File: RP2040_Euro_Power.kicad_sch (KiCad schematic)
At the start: 150 parts, among them J1 Conn_01x40, J2 Conn_01x40, J3 Power, J4 USB C/USB 2.0, J5 Conn_01x03_Pin, SW1 SW_BOOT, SW2 SW_RESET, U1 78L05_SOT89, U2 W25Q128JVS, U3 TL431D, U4 AMS1117-3.3, U5 RP2040, U6 MCP6002, Y1 Crystal_12MHz_4Pin

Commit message: half of the parts placed on board
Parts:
- removed JP127, JP128, JP129, JP130: ~, Jumper:SolderJumper-2_P1.3mm_Bridged_RoundedPad1.0x1.5mm, symbol Jumper:SolderJumper_2_Bridged
- removed U6: MCP6002, Package_SO:SOIC-8_3.9x4.9mm_P1.27mm, symbol winterbloom:MCP6002
- added C25: 100n, winterbloom:C_0603_HandSolder, symbol DecapodDevices:C_Small
- added D11, D13: D_Schottky, winterbloom:D_SMA, symbol Diode:1N5819
- added JP127, JP128, JP129, JP130: SolderJumper_2_Open, Jumper:SolderJumper-2_P1.3mm_Open_RoundedPad1.0x1.5mm, symbol Jumper:SolderJumper_2_Open
- added U7: TL072, Package_SO:SOIC-8_3.9x4.9mm_P1.27mm, symbol Amplifier_Operational:TL072
- R8: value 33k -> 47k
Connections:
- net GND_PLANE is gone; now on net GND: JP133.2 (B), JP134.2 (B), JP173.1 (A), JP174.1 (A)
- net RUN is gone; now on net D29: R6.1, SW2.1 (A), U5.26 (RUN)
- net SWCLK is gone; now on net D27: J5.1 (Pin_1), U5.24 (SWCLK)
- net SWD is gone; now on net D28: J5.3 (Pin_3), U5.25 (SWD)
- net +12V: now also C19.1, D2.2 (A), D11.1 (K), U7.8 (V+); no longer R16.1
- net +3.3V: now also D10.2 (A); no longer R20.1
- net +5V: now also D8.2 (A); no longer C19.1, R18.1
- net -12V: now also D7.1 (K), C25.1, D13.2 (A), U7.4 (V-); no longer R17.1
- net D27: now also JP127.1 (A)
- net D28: now also JP128.1 (A)
- net D29: now also JP129.1 (A)
- net GND: now also R16.2, R17.2, R18.2, R19.2, R20.2, C25.2, U7.5 (+); no longer D10.1 (K), D2.1 (K), D7.2 (A), D8.1 (K), D9.1 (K)
- net VBUS: now also D9.2 (A); no longer R19.1
- net at J1.27 (Pin_27): now also JP127.2 (B)
- net at R9.2, U3.1 (K), U3.8 (REF): now also U7.3 (+)
- net at C22.1, R7.1, R8.2: now also U7.2 (-)
- net BOOT: now reaches R2.1, R3.2, R5.1, SW1.1 (A)
- net BOOT: now also JP130.1 (A)
- net at J1.28 (Pin_28): now also JP128.2 (B)
- net at J1.29 (Pin_29): now also JP129.2 (B)
- net at J1.30 (Pin_30): now also JP130.2 (B)
- net at D3.2 (A), FB1.1: now also D13.1 (K)
- net at D4.1 (K), FB2.1: now also D11.2 (A)
- net 3.3VREF renamed 3VREF
- net 3VREF: now also U7.1
- new net: D9.1 (K), R19.1
- new net: D7.2 (A), R17.1
- new net: D2.1 (K), R16.1
- new net: D10.1 (K), R20.1
- new net: D8.1 (K), R18.1
- new net: U7.6 (-), U7.7
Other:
- note added: "Find a use for the extra op amp? Prototyping area if extra space? Add Default/RGB LEDs? Add any niceties for this situation?"
- note added: "No Obvious Problems"
- note removed: "Add Power LEDs Find a use for the extra op amp? Prototyping area if extra space? Figure out SWD/debug stuff"
- note removed: "How should I power 3.3vref buffer? If I use 3.3vreg, I have no headroom for stability If I use 5v, I have to have USB Connected? If I use 12v, op amp will blow up."
- moved on the sheet: C19, C20, C21, C23, C24, C5, C6, C7, C8, D10, D2, D3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

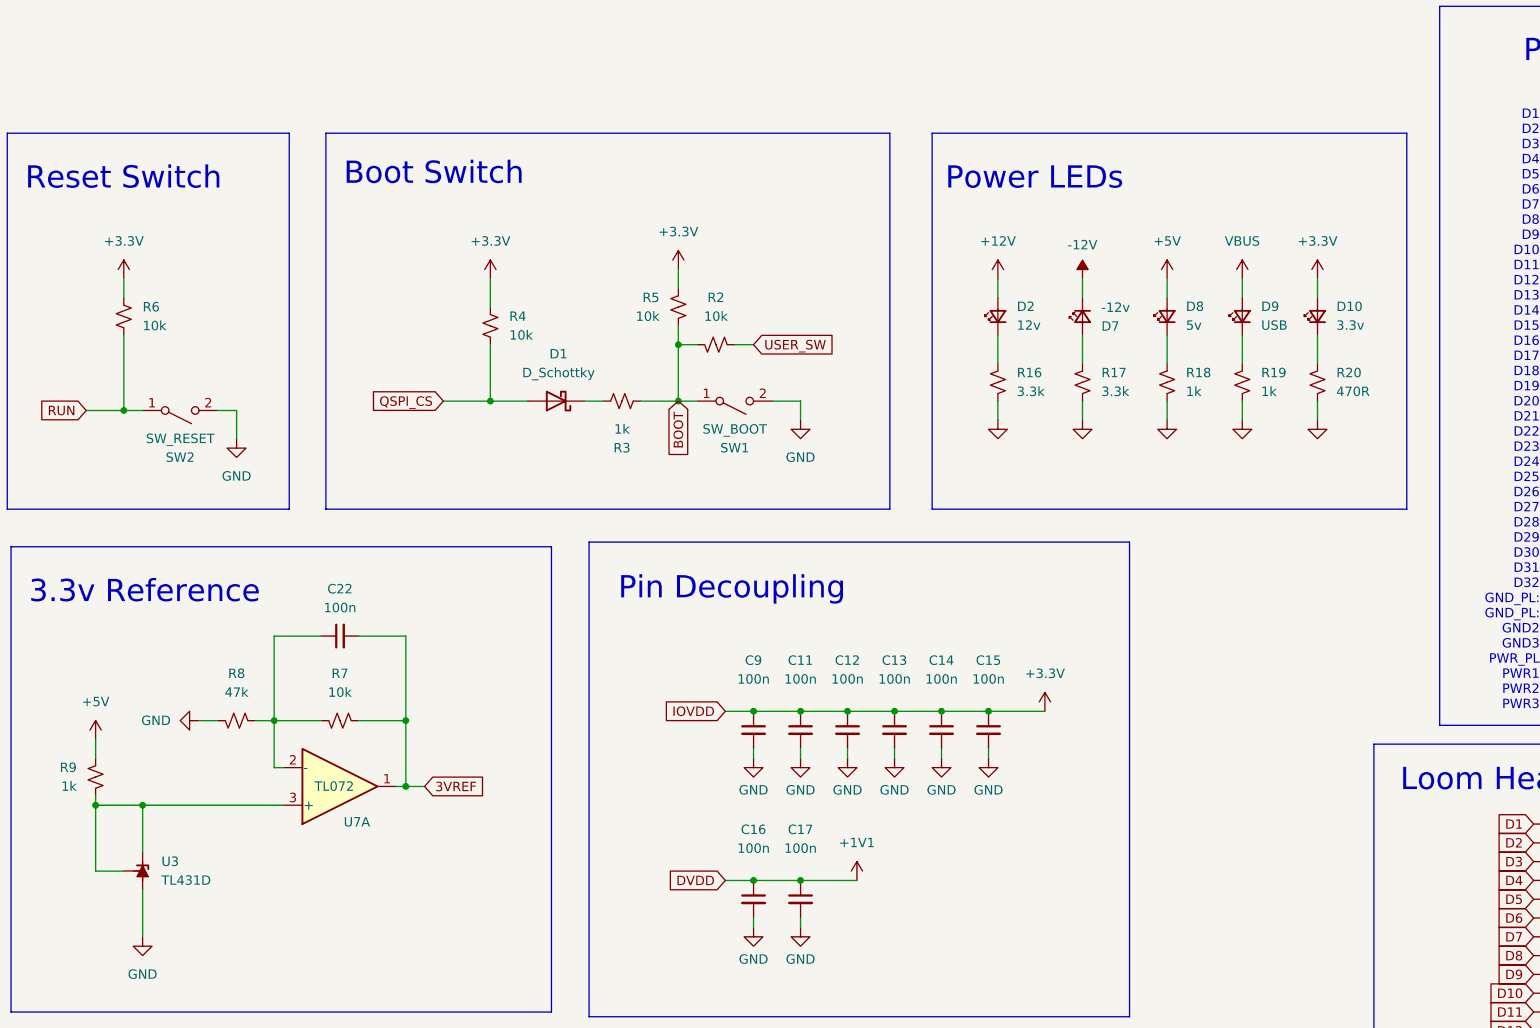
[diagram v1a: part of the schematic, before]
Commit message: all parts placed on board
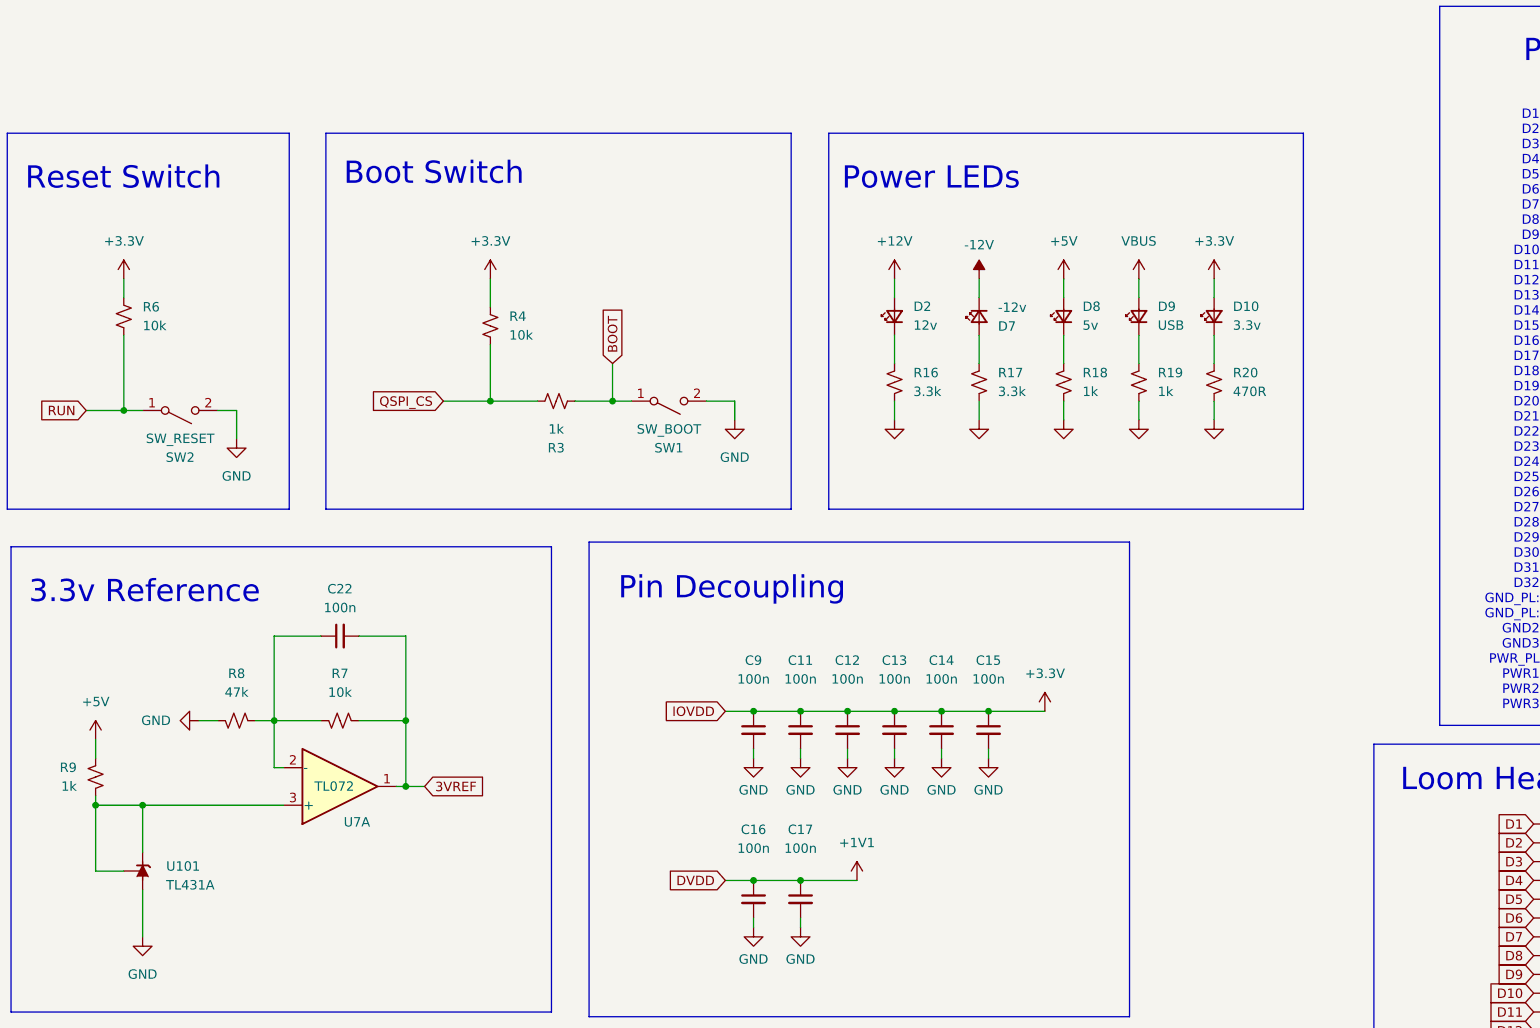
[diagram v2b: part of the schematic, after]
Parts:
- removed D1: D_Schottky, winterbloom:D_SMA, symbol Device:D_Schottky
- removed R2, R5: 10k, winterbloom:R_0603_HandSolder, symbol DecapodDevices:R_Small_US
- removed U3: TL431D, Package_SO:SOIC-8_3.9x4.9mm_P1.27mm, symbol Reference_Voltage:TL431D
- added U101: TL431A, Package_TO_SOT_SMD:SOT-23, symbol Reference_Voltage:TL431DBZ
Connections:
- net GND: now also U101.3 (A)
- net QSPI_CS: now also R3.1
- net at R9.2, U7.3 (+): now also U101.1 (K), U101.2 (REF)
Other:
- moved on the sheet: D10, D2, D7, D8, D9, R16, R17, R18, R19, R20, R3, SW1

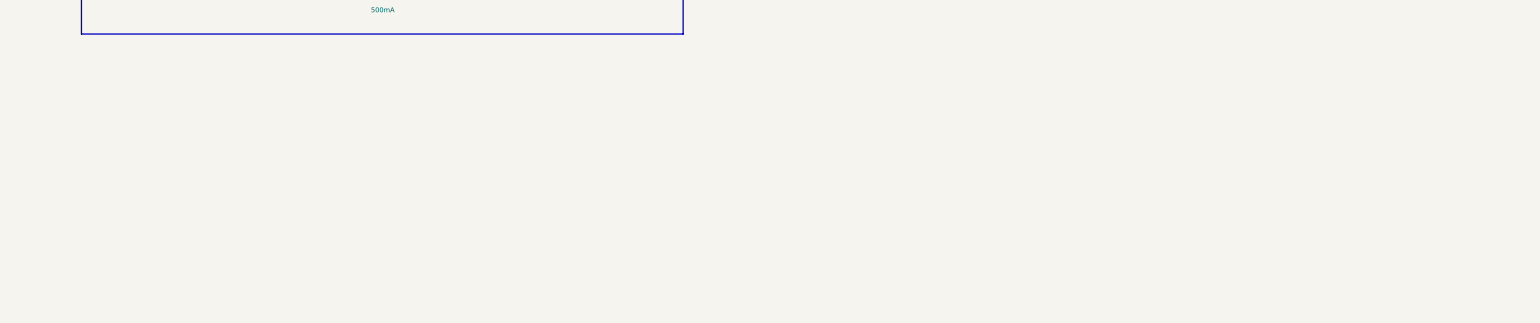
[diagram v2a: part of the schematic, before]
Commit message: Board mostly layed out, ready to start routing
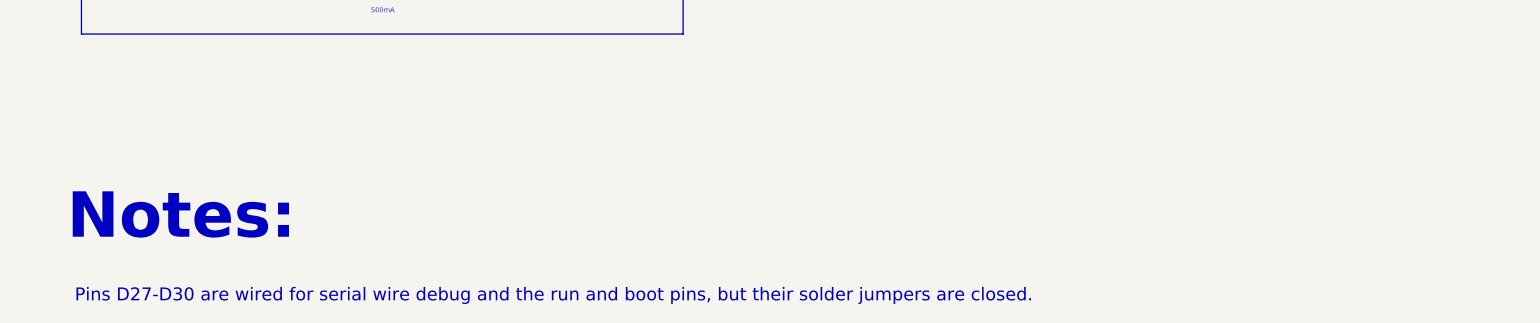
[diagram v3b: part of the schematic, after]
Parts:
- JP127, JP128, JP129, JP130: footprint Jumper:SolderJumper-2_P1.3mm_Open_RoundedPad1.0x1.5mm -> Jumper:SolderJumper-2_P1.3mm_Open_Pad1.0x1.5mm
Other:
- note added: "Notes:"
- note added: "Pins D27-D30 are wired for serial wire debug and the run and boot pins, but their solder jumpers are closed."
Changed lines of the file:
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@@
 		)
 	)
+	(text "Notes:"
+		(exclude_from_sim no)
+		(at 23.368 287.782 0)
+		(effects
+			(font
+				(size 6 6)
+				(thickness 0.8)
+				(bold yes)
+			)
+			(justify left)
+		)
+	)
 	(text "Unused Op Amp"
 		(exclude_from_sim no)
@@
 		)
 	)
+	(text "Pins D27-D30 are wired for serial wire debug and the run and boot pins, but their solder jumpers are closed."
+		(exclude_from_sim no)
+		(at 24.384 297.18 0)
+		(effects
+			(font
+				(size 1.7 1.7)
+			)
+			(justify left top)
+		)
+	)
 	(global_label "D23"
 		(shape input)
@@
 			)
 		)
-		(property "Footprint" "Jumper:SolderJumper-2_P1.3mm_Open_RoundedPad1.0x1.5mm"
+		(property "Footprint" "Jumper:SolderJumper-2_P1.3mm_Open_Pad1.0x1.5mm"
 			(at 368.3 199.39 0)
 			(effects
@@
 			)
 		)
-		(property "Footprint" "Jumper:SolderJumper-2_P1.3mm_Open_RoundedPad1.0x1.5mm"
+		(property "Footprint" "Jumper:SolderJumper-2_P1.3mm_Open_Pad1.0x1.5mm"
 			(at 368.3 191.77 0)
 			(effects
@@
 			)
 		)
-		(property "Footprint" "Jumper:SolderJumper-2_P1.3mm_Open_RoundedPad1.0x1.5mm"
+		(property "Footprint" "Jumper:SolderJumper-2_P1.3mm_Open_Pad1.0x1.5mm"
 			(at 368.3 196.85 0)
 			(effects
@@
 			)
 		)
-		(property "Footprint" "Jumper:SolderJumper-2_P1.3mm_Open_RoundedPad1.0x1.5mm"
+		(property "Footprint" "Jumper:SolderJumper-2_P1.3mm_Open_Pad1.0x1.5mm"
 			(at 368.3 194.31 0)
 			(effects

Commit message: Second op amp used. Ready for routing
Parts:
- added C26: DNP, winterbloom:C_0603_HandSolder, symbol Device:C_Small
- added D1, D12: D_Schottky, winterbloom:D_SMA, symbol Diode:1N5819
- added JP1, JP201: Jumper_Closed, Jumper:SolderJumper-2_P1.3mm_Bridged_RoundedPad1.0x1.5mm, symbol Jumper:SolderJumper_2_Bridged
- added JP2, JP3, JP4: SolderJumper_2_Open, Jumper:SolderJumper-2_P1.3mm_Open_Pad1.0x1.5mm, symbol Jumper:SolderJumper_2_Open
- added R2, R21, R22, R23, R24, R26, R5: DNP, winterbloom:R_0603_HandSolder, symbol DecapodDevices:R_Small_US
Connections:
- net +3.3V: now also JP3.2 (B)
- net A28: now also R26.1
- net A29: now also JP2.2 (B), R5.1
- net A30: now also R21.1, R24.2
- net A31: now also R24.1
- net A32: now also D1.2 (A), D12.1 (K), R23.2
- net GND: now also JP2.1 (A), JP4.1 (A), R22.1; no longer U7.5 (+)
- net QSPI_CS: now also U2.1 (~{CS}), U5.56 (QSPI_SS)
- net at U7.6 (-): now also JP1.1 (A), R2.1, R5.2; no longer U7.7
- new net: C26.2, JP201.2 (B), R2.2
- new net: C26.1, JP1.2 (B), R26.2
- new net: JP201.1 (A), R23.1, U7.7
- new net: D12.2 (A), JP4.2 (B)
- new net: R21.2, R22.2, U7.5 (+)
- new net: D1.1 (K), JP3.1 (A)
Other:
- note added: "Op Amp Possibilities: Low pass filter for PWM/delta sigma DAC comparator for analog voltage threshold detection Level converter for CV input"
- note added: "Pin Connections"
- note added: "Pins D27-D30 are wired for serial wire debug and the run and boot pins, but their solder jumpers are closed. Open Solder Jumpers are square, closed are circular"
- note added: "Prototyping area if extra space? Add Default/RGB LEDs? Add any pin protection? USB? gpio? Test Points? Are all the required test points already exposed to pins?"
- note added: "Reconfigurable Op Amp"
- note removed: "Find a use for the extra op amp? Prototyping area if extra space? Add Default/RGB LEDs? Add any niceties for this situation?"
- note removed: "Pins D27-D30 are wired for serial wire debug and the run and boot pins, but their solder jumpers are closed."
- note removed: "Unused Op Amp"
- moved on the sheet: C11, C12, C13, C14, C15, C16, C17, C19, C20, C21, C22, C23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

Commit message: Loom RP2040 V1 Ordered
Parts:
- JP101, JP102, JP103, JP104, JP105, JP106, JP107, JP108, JP109, JP110, JP111, JP112, JP113, JP114, JP115, JP116, JP117, JP118, JP119, JP120, JP121, JP122, JP123, JP124, JP125, JP126, JP131, JP132, JP133, JP134, JP135, JP136, JP137, JP138, JP139, JP140, JP141, JP142, JP143, JP144, JP145, JP146, JP147, JP148, JP149, JP150, JP151, JP152, JP153, JP154, JP155, JP156, JP157, JP158, JP159, JP160, JP161, JP162, JP163, JP164, JP165, JP166, JP167, JP168, JP169, JP170, JP171, JP172, JP173, JP174, JP175, JP176, JP177, JP178, JP179, JP180: footprint Jumper:SolderJumper-2_P1.3mm_Bridged_RoundedPad1.0x1.5mm -> Decapod_Devices:SolderJumper-2_P1.3mm_Bridged_RoundedPad1.0x1.5mm
- JP127, JP128, JP129, JP130: footprint Jumper:SolderJumper-2_P1.3mm_Open_Pad1.0x1.5mm -> Decapod_Devices:SolderJumper-2_P1.3mm_Open_Pad1.0x1.5mm
- R1, R18, R19, R3, R9: LCSC (none) -> C21190; MPN (none) -> 0603WAF1001T5E; Manufacturer (none) -> UNI-ROYAL(Uniroyal Elec)
- R10, R11: LCSC (none) -> C25190; MPN (none) -> 0603WAF270JT5E; Manufacturer (none) -> UNI-ROYAL(Uniroyal Elec)
- R12, R13: LCSC (none) -> C23186; MPN (none) -> 0603WAF5101T5E; Manufacturer (none) -> UNI-ROYAL(Uniroyal Elec)
- R14: LCSC (none) -> C22936; MPN (none) -> 0603WAF100KT5E; Manufacturer (none) -> UNI-ROYAL(Uniroyal Elec)
- R15: LCSC (none) -> C8218; MPN (none) -> 0603WAF2000T5E; Manufacturer (none) -> UNI-ROYAL(Uniroyal Elec)
- R16, R17: LCSC (none) -> C22978; MPN (none) -> 0603WAF3301T5E; Manufacturer (none) -> UNI-ROYAL(Uniroyal Elec)
- R20: LCSC (none) -> C23179; MPN (none) -> 0603WAF4700T5E; Manufacturer (none) -> UNI-ROYAL(Uniroyal Elec)
- R4, R6, R7: LCSC (none) -> C25804; MPN (none) -> 0603WAF1002T5E; Manufacturer (none) -> UNI-ROYAL(Uniroyal Elec)
- R8: LCSC (none) -> C25819; MPN (none) -> 0603WAF4702T5E; Manufacturer (none) -> UNI-ROYAL(Uniroyal Elec)
- U7: LCSC (none) -> C6961; MPN (none) -> TL072CDT; Manufacturer (none) -> STMicroelectronics
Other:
- note added: "3v Reference"
- note removed: "3.3v Reference"
- note removed: "Op Amp Possibilities: Low pass filter for PWM/delta sigma DAC comparator for analog voltage threshold detection Level converter for CV input"
